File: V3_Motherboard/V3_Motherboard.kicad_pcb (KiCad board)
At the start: 2 copper layers, 135.3 x 55.5 mm, 64 parts, among them J1 Conn_01x16_Pin, J10 Conn_02x04_Row_Letter_First, J14_GND2 Conn_01x03, J14_GND3 Conn_01x03, J18_VDC1 Conn_01x02, J2 Conn_01x16_Pin, J3 Conn_01x16_Pin, J4 Conn_01x16_Pin, J5 PINHD_1x2_Male, J6 Conn_01x02_Pin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

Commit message: Modded
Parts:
- J9: value Conn_02x03_Counter_Clockwise -> Conn_01x05_Pin; footprint Connector_PinHeader_2.54mm:PinHeader_2x03_P2.54mm_Vertical -> Connector_PinHeader_2.54mm:PinHeader_1x05_P2.54mm_Vertical
- moved J9 14.2 mm to (165.1, 101.6), turned to -90 degrees
- moved G*** 5.00 mm to (165.5, 94.0)
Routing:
- net ISINK_REF: track 77.9 -> 70.4 mm
- net /BUS1: track 18.4 -> 22.8 mm, vias 1 -> 2
- net /BUS4: track 32.5 -> 28.7 mm, vias 3 -> 2
- net /BUS2: track 28.4 -> 25.2 mm, vias 3 -> 2
- net /BUS5: track 31.3 -> 30.8 mm, vias 3 -> 2
- net /BUS3: track 27.4 -> 27.3 mm, vias 3 -> 2
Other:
- board text added: "20260418"
- board text added: "PCB V4A Rev A"
- board text added: "Serial Number"
- board text removed: "20250207"

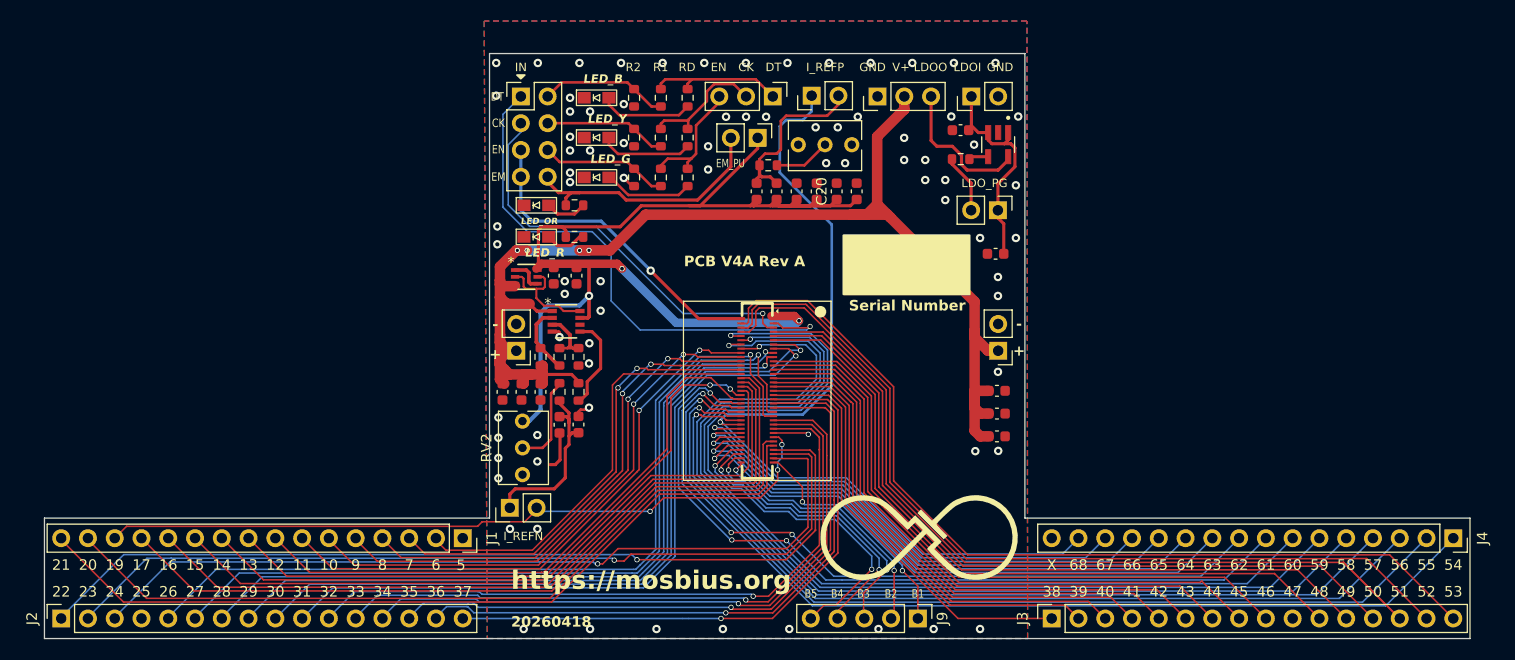
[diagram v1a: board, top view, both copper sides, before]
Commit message: Simplified PCB without LDO and additional breakouts
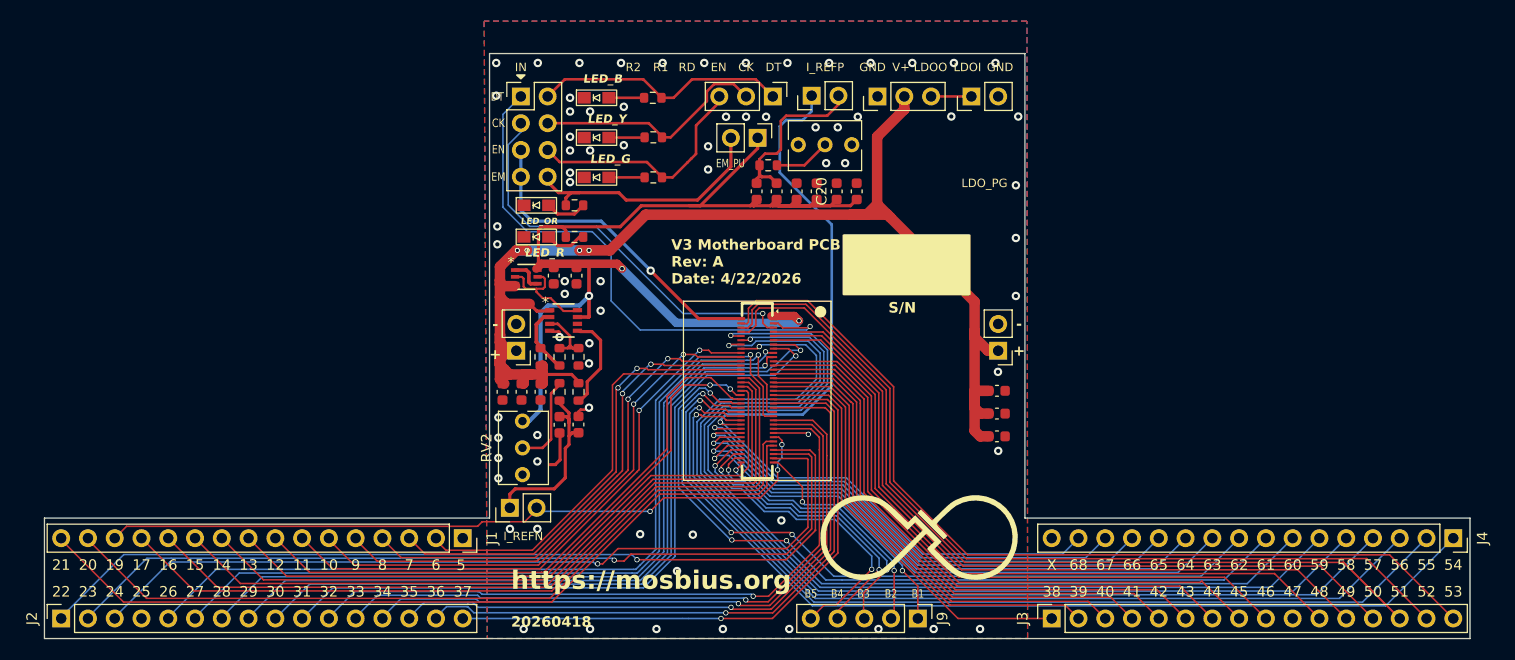
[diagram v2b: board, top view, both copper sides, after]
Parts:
- removed C4: 1u, Capacitor_SMD:C_0603_1608Metric
- removed C5: 10u, Capacitor_SMD:C_0603_1608Metric
- removed JP1_LDOPG1: Jumper_2_Open, Connector_PinHeader_2.54mm:PinHeader_1x02_P2.54mm_Vertical
- removed R1, R3, R5: 1.1k, Resistor_SMD:R_0603_1608Metric
- removed R10: 10K, Resistor_SMD:R_0603_1608Metric
- removed R2, R4, R6: 3.3k, Resistor_SMD:R_0603_1608Metric
- removed U1: NCV8164ASN250T1G_LDO_2.5V, E6350_23:NCV8164ASN250T1G
- moved R9 3.31 mm to (139.9, 52.2), turned to 180 degrees
- moved R8 3.26 mm to (140.0, 56.0), turned to 180 degrees
- moved R7 3.26 mm to (140.0, 59.8), turned to 180 degrees
- moved U2 0.25 mm to (131.5, 73.3)
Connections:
- net EN_MAN_2.5V renamed EN_MAN_3.3V
- J10 pad 2: DATA_CVRT_2.5V -> DATA_CVRT_3.3V
- J10 pad 4: CLK_CVRT_2.5V -> CLK_CVRT_3.3V
- J10 pad 6: EN_CVRT_2.5V -> EN_CVRT_3.3V
- J14_GND3 pad 3: LDO_OUT_2.5V -> VIN
- J18_VDC1 pad 1: LDO_VIN -> VIN
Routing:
- net LDO_VIN: track 20.9 -> 0.00 mm
- net LDO_OUT_2.5V: track 13.6 -> 0.00 mm
- net DATA_CVRT_2.5V: track 12.2 -> 0.00 mm
- net EN_CVRT_2.5V: track 11.9 -> 0.00 mm
- net CLK_CVRT_2.5V: track 11.6 -> 0.00 mm
- net DATA_CVRT_3.3V: track 13.1 -> 24.1 mm
- net EN_CVRT_3.3V: track 11.0 -> 21.8 mm
- net CLK_CVRT_3.3V: track 11.7 -> 22.5 mm
- net Net-(JP1_LDOPG1-B): track 5.60 -> 0.00 mm
- net Net-(D4-A): track 8.88 -> 3.36 mm
- net Net-(D3-A): track 8.81 -> 3.42 mm
- net Net-(D2-A): track 8.34 -> 3.36 mm
- net VIN: track 0.00 -> 3.86 mm
- net LDO_PG_2.5V: track 1.88 -> 0.00 mm
- net GND: track 10.9 -> 9.83 mm, vias 79 -> 72
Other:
- board text added: "S/N"
- board text added: "V3 Motherboard PCB Rev: A Date: 4/22/2026"
- board text removed: "PCB V4A Rev A"
- board text removed: "Serial Number"

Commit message: New Push
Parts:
- moved C20 12.8 mm to (153.4, 73.2), turned to 0 degrees
- moved C17 1.90 mm to (157.4, 61.1)
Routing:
- net VDD: track 114.0 -> 104.1 mm
- net GND: track 9.83 -> 8.09 mm, vias 72 -> 74
- net /NMOS_4B_GATE: track 71.5 -> 70.2 mm
- net /NMOS_4B_DRAIN: track 67.9 -> 69.1 mm
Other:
- board text added: "CK-E"
- board text added: "DT-E"
- board text added: "EN-E"
- board text added: "V3 Motherboard PCB Rev: A Date: 4/23/2026"
- board text added: "VIN"
- board text removed: "LDOI"
- board text removed: "LDOO"
- board text removed: "LDO_PG"
- board text removed: "V3 Motherboard PCB Rev: A Date: 4/22/2026"

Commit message: New Push
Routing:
- net GND: track 8.09 -> 9.32 mm, vias 74 -> 86
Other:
- board text added: "20260423"
- board text added: "V3 Motherboard PCB Rev: A"
- board text removed: "20260418"
- board text removed: "V3 Motherboard PCB Rev: A Date: 4/23/2026"
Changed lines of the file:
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@@
 		)
 	)
-	(gr_text "20260418"
+	(gr_text "20260423"
 		(at 126.5 102.5 0)
 		(layer "F.SilkS")
@@
 		)
 	)
-	(gr_text "V3 Motherboard PCB\nRev: A\nDate: 4/23/2026"
+	(gr_text "V3 Motherboard PCB\nRev: A"
 		(at 157.75 68.35 0)
 		(layer "F.SilkS")
@@
 	)
 	(segment
-		(start 133.712 81.788)
-		(end 133.9 81.6)
-		(width 0.25)
+		(start 153.95 84.6)
+		(end 153.35 84)
+		(width 0.15)
 		(layer "F.Cu")
 		(net 2)
 	)
 	(segment
-		(start 152.851018 84.4)
-		(end 152.726018 84.275)
-		(width 0.15)
+		(start 133.712 81.788)
+		(end 133.9 81.6)
+		(width 0.25)
 		(layer "F.Cu")
 		(net 2)
@@
 	)
 	(segment
+		(start 153.35 84)
+		(end 151.35 84)
+		(width 0.15)
+		(layer "F.Cu")
+		(net 2)
+	)
+	(segment
 		(start 133.096 81.788)
 		(end 133.712 81.788)
@@
 	)
 	(segment
-		(start 152.451018 84)
-		(end 152.726018 84.275)
-		(width 0.15)
-		(layer "F.Cu")
-		(net 2)
-	)
-	(segment
 		(start 131.1 84)
 		(end 131.15 84.05)
@@
 	)
 	(segment
-		(start 151.4 84)
-		(end 152.451018 84)
-		(width 0.15)
-		(layer "F.Cu")
-		(net 2)
-	)
-	(segment
 		(start 131.1 74.9)
 		(end 131.1 74.458)
@@
 	)
 	(via
+		(at 154.75 84.4)
+		(size 0.5)
+		(drill 0.35)
+		(layers "F.Cu" "B.Cu")
+		(net 2)
+	)
+	(via
 		(at 156.4 58.4)
 		(size 0.8)
@@
 	)
 	(via
+		(at 166.9 80.25)
+		(size 0.8)
+		(drill 0.4)
+		(layers "F.Cu" "B.Cu")
+		(free yes)
+		(net 2)
+	)
+	(via
 		(at 143.75 93.65)
 		(size 0.8)
@@
 	)
 	(via
+		(at 153.15 84.45)
+		(size 0.5)
+		(drill 0.35)
+		(layers "F.Cu" "B.Cu")
+		(net 2)
+	)
+	(via
 		(at 135 69.6)
 		(size 0.8)
@@
 	)
 	(via
+		(at 143.55 67.95)
+		(size 0.8)
+		(drill 0.4)
+		(layers "F.Cu" "B.Cu")
+		(free yes)
+		(net 2)
+	)
+	(via
 		(at 125.1 52)
 		(size 0.8)
@@
 	)
 	(via
-		(at 152.726018 84.275)
+		(at 153.95 84.6)
 		(size 0.8)
 		(drill 0.4)
@@
 	)
 	(via
+		(at 154.25 67.95)
+		(size 0.8)
+		(drill 0.4)
+		(layers "F.Cu" "B.Cu")
+		(free yes)
+		(net 2)
+	)
+	(via
 		(at 168.518413 48.895)
 		(size 0.8)
@@
 	)
 	(via
+		(at 154.75 85.05)
+		(size 0.5)
+		(drill 0.35)
+		(layers "F.Cu" "B.Cu")
+		(net 2)
+	)
+	(via
 		(at 171 102.6)
 		(size 0.8)
@@
 	)
 	(via
+		(at 153.15 85.05)
+		(size 0.5)
+		(drill 0.35)
+		(layers "F.Cu" "B.Cu")
+		(net 2)
+	)
+	(via
 		(at 129 86.7)
 		(size 0.8)
@@
 	)
 	(via
+		(at 165.7 75.45)
+		(size 0.8)
+		(drill 0.4)
+		(layers "F.Cu" "B.Cu")
+		(free yes)
+		(net 2)
+	)
+	(via
 		(at 148.780498 48.895)
 		(size 0.8)
@@
 	)
 	(via
+		(at 160.85 71.15)
+		(size 0.8)
+		(drill 0.4)
+		(layers "F.Cu" "B.Cu")
+		(free yes)
+		(net 2)
+	)
+	(via
+		(at 168.65 88.8)
+		(size 0.8)
+		(drill 0.4)
+		(layers "F.Cu" "B.Cu")
+		(free yes)
+		(net 2)
+	)
+	(via
 		(at 126.4 93.1)
 		(size 0.8)
@@
 	)
 	(via
+		(at 166.95 84.85)
+		(size 0.8)
+		(drill 0.4)
+		(layers "F.Cu" "B.Cu")
+		(free yes)
+		(net 2)
+	)
+	(via
 		(at 125.3 88.3)
 		(size 0.8)
@@
 		(size 0.8)
 		(drill 0.4)
+		(layers "F.Cu" "B.Cu")
+		(free yes)
+		(net 2)
+	)
+	(via
+		(at 149.6 67.95)
+		(size 0.8)
+		(drill 0.4)
